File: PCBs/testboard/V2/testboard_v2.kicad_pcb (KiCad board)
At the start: 2 copper layers, 70 x 59 mm, 39 parts, among them J1 FLEX pin1, J10 Conn_01x01, J11 Conn_01x01, J12 Conn_01x01, J13 Conn_01x02_Socket, J2 FLEX pin2, J3 FSR pin2, J4 FSR pin1, J5 Conn_01x02_Socket, J9 Conn_01x01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

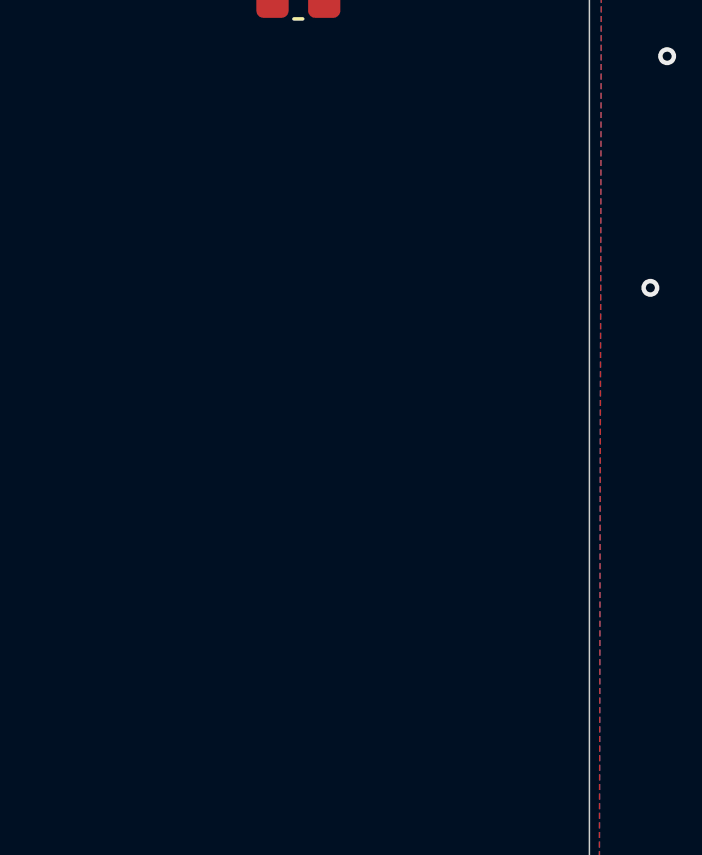
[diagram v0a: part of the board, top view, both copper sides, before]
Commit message: V2 updated for USB
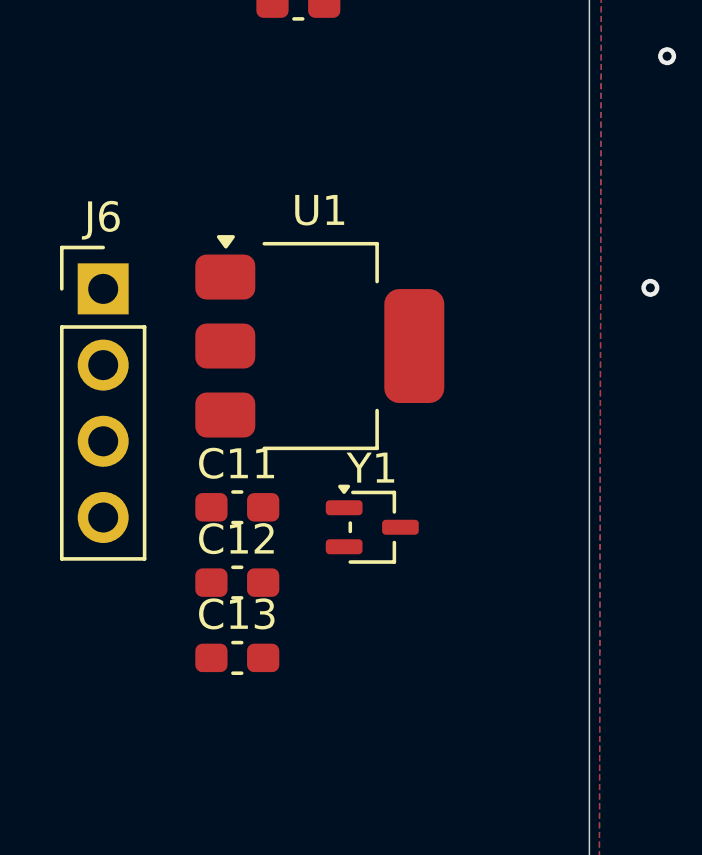
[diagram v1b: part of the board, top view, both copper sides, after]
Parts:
- added C11: 22uF, Capacitor_SMD:C_0603_1608Metric_Pad1.08x0.95mm_HandSolder, F.Cu at (121.6, 113.3)
- added C12: 10uF, Capacitor_SMD:C_0603_1608Metric_Pad1.08x0.95mm_HandSolder, F.Cu at (121.6, 115.8)
- added C13: 0.1uF, Capacitor_SMD:C_0603_1608Metric_Pad1.08x0.95mm_HandSolder, F.Cu at (121.6, 118.4)
- added J6: USB_Conn, Connector_PinHeader_2.54mm:PinHeader_1x04_P2.54mm_Vertical, F.Cu at (117.1, 106.1)
- added U1: LD1117S33TR_SOT223, Package_TO_SOT_SMD:SOT-223-3_TabPin2, F.Cu at (124.3, 108.0)
- added Y1: MAX7375AXR805, Package_TO_SOT_SMD:SOT-323_SC-70, F.Cu at (126.1, 114.0)
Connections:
- U2 pad 41: unconnected-(U2-PA8-Pad41) -> /DEBUG_1
- U2 pad 42: /DEBUG_1 -> /USB_VBUS_5V
- U2 pad 44: unconnected-(U2-PA11-Pad44) -> /USB_D-
- U2 pad 45: unconnected-(U2-PA12-Pad45) -> /USB_D+
- U2 pad 5: unconnected-(U2-PH0-Pad5) -> /PH0

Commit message: V2 schematic done - awaiting layout from kenobi
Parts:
- added R1: 22 Ohm, Capacitor_SMD:C_0603_1608Metric_Pad1.08x0.95mm_HandSolder, F.Cu at (101.9, 104.5)
- added R2: 22 Ohm, Capacitor_SMD:C_0603_1608Metric_Pad1.08x0.95mm_HandSolder, F.Cu at (101.9, 111.0)
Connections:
- J6 pad 2: /USB_D- -> Net-(J6-Pin_2)
- J6 pad 3: /USB_D+ -> Net-(J6-Pin_3)

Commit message: Finalboard-V1 layout done (by kenobi)
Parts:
- moved R1 46.0 mm to (145.6, 90.0), turned to 180 degrees
- moved Y1 43.3 mm to (159.7, 86.7)
- moved R2 39.9 mm to (141.6, 107.1), turned to 180 degrees
- moved U1 39.5 mm to (143.2, 73.3)
- moved C13 36.1 mm to (136.7, 85.6)
- moved C9 35.9 mm to (154.4, 75.5)
- moved C11 34.8 mm to (136.4, 81.9)
- moved U4 34.1 mm to (156.5, 81.2)
- moved C10 32.2 mm to (151.5, 80.4)
- moved C12 31.0 mm to (136.7, 88.8)
- moved J6 25.1 mm to (138.7, 93.3)
- moved 1k2 6.91 mm to (161.9, 79.6)
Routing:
- net VCC: track 186.8 -> 259.9 mm, vias 4 -> 8
- net /USB_VBUS_5V: track 0.00 -> 60.7 mm, vias 0 -> 2
- net /USB_D+: track 0.00 -> 36.8 mm, vias 0 -> 2
- net /SDA_1.8V: track 43.4 -> 7.96 mm
- net /SCL: track 33.9 -> 0.00 mm, vias 6 -> 0
- net /USB_D-: track 0.00 -> 32.4 mm, vias 0 -> 4
- net /SPI_SCK: track 0.00 -> 26.9 mm, vias 0 -> 2
- net /SPI_MOSI: track 0.00 -> 25.0 mm, vias 0 -> 2
- net /SPI_MISO: track 0.00 -> 21.1 mm, vias 0 -> 2
- net /IMU_INT1_TEST: track 0.00 -> 20.8 mm, vias 0 -> 2
- net /SPI_CS: track 0.00 -> 18.3 mm, vias 0 -> 2
- net /VLDO_OUT: track 86.3 -> 68.4 mm
- net /SDA: track 34.6 -> 16.7 mm, vias 2 -> 0
- net /SCL_1.8V: track 15.4 -> 0.00 mm
- net /PH0: track 0.00 -> 13.1 mm, vias 0 -> 2
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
